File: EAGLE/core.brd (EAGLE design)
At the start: 20.3 x 33 mm, 47 parts, among them Q1 MMDT3904, U1 MIC5219, U3 STM32F10XCXT6, U4 SST25VF040B-50-4I-S2AF, X1 USB-MICROB, Y1 8Mhz

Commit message: Finished Core Debug v0.0.8
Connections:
- net SPI_MISO: no longer U2.SPI_DIN
- net SPI_MOSI: now also U2.SPI_DIN
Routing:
- net SPI_MISO: track 27.2 -> 26.7 mm
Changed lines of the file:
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@@
 <setting verticaltext="up"/>
 </settings>
-<grid distance="0.005" unitdist="inch" unit="inch" style="lines" multiple="1" display="yes" altdistance="0.005" altunitdist="inch" altunit="inch"/>
+<grid distance="0.05" unitdist="inch" unit="inch" style="lines" multiple="1" display="yes" altdistance="0.005" altunitdist="inch" altunit="inch"/>
 <layers>
-<layer number="1" name="Top" color="4" fill="1" visible="no" active="yes"/>
+<layer number="1" name="Top" color="4" fill="1" visible="yes" active="yes"/>
 <layer number="2" name="$GND" color="13" fill="1" visible="no" active="yes"/>
 <layer number="3" name="Route3" color="4" fill="3" visible="no" active="no"/>
@@
 <layer number="14" name="Route14" color="1" fill="6" visible="no" active="no"/>
 <layer number="15" name="$+3V3" color="11" fill="1" visible="no" active="yes"/>
-<layer number="16" name="Bottom" color="1" fill="1" visible="no" active="yes"/>
+<layer number="16" name="Bottom" color="1" fill="1" visible="yes" active="yes"/>
 <layer number="17" name="Pads" color="2" fill="1" visible="yes" active="yes"/>
-<layer number="18" name="Vias" color="2" fill="1" visible="no" active="yes"/>
-<layer number="19" name="Unrouted" color="6" fill="1" visible="no" active="yes"/>
+<layer number="18" name="Vias" color="2" fill="1" visible="yes" active="yes"/>
+<layer number="19" name="Unrouted" color="6" fill="1" visible="yes" active="yes"/>
 <layer number="20" name="Dimension" color="6" fill="1" visible="yes" active="yes"/>
 <layer number="21" name="tPlace" color="16" fill="1" visible="yes" active="yes"/>
-<layer number="22" name="bPlace" color="14" fill="1" visible="no" active="yes"/>
+<layer number="22" name="bPlace" color="14" fill="1" visible="yes" active="yes"/>
 <layer number="23" name="tOrigins" color="15" fill="1" visible="yes" active="yes"/>
-<layer number="24" name="bOrigins" color="15" fill="1" visible="no" active="yes"/>
+<layer number="24" name="bOrigins" color="15" fill="1" visible="yes" active="yes"/>
 <layer number="25" name="tNames" color="7" fill="1" visible="no" active="yes"/>
 <layer number="26" name="bNames" color="7" fill="1" visible="no" active="yes"/>
-<layer number="27" name="tValues" color="7" fill="1" visible="yes" active="yes"/>
+<layer number="27" name="tValues" color="7" fill="1" visible="no" active="yes"/>
 <layer number="28" name="bValues" color="7" fill="1" visible="no" active="yes"/>
 <layer number="29" name="tStop" color="7" fill="3" visible="no" active="yes"/>
 <layer number="30" name="bStop" color="7" fill="6" visible="no" active="yes"/>
-<layer number="31" name="tCream" color="7" fill="4" visible="yes" active="yes"/>
+<layer number="31" name="tCream" color="7" fill="4" visible="no" active="yes"/>
 <layer number="32" name="bCream" color="7" fill="5" visible="no" active="yes"/>
 <layer number="33" name="tFinish" color="6" fill="3" visible="no" active="yes"/>
@@
 <signal name="SPI_MISO">
 <contactref element="U2" pad="SPI_DOUT"/>
-<contactref element="U2" pad="SPI_DIN"/>
 <contactref element="U3" pad="27"/>
 <contactref element="U4" pad="2"/>
@@
 <wire x1="11.938" y1="18.034" x2="11.938" y2="18.161" width="0.2032" layer="1"/>
 <wire x1="11.938" y1="18.161" x2="11.43" y2="18.669" width="0.2032" layer="1"/>
-<wire x1="9.56" y1="19.92" x2="9.56" y2="20.482" width="0.2032" layer="1"/>
 <wire x1="9.56" y1="20.482" x2="9.906" y2="20.828" width="0.2032" layer="1"/>
 <wire x1="9.906" y1="20.828" x2="11.684" y2="20.828" width="0.2032" layer="1"/>
@@
 <wire x1="10.16" y1="17.653" x2="10.287" y2="17.526" width="0.2032" layer="16"/>
 <wire x1="10.287" y1="17.526" x2="11.43" y2="17.526" width="0.2032" layer="16"/>
+<contactref element="U2" pad="SPI_DIN"/>
+<wire x1="10.16" y1="17.653" x2="9.56" y2="19.92" width="0" layer="19" extent="1-16"/>
 </signal>
 <signal name="USB_DISC">

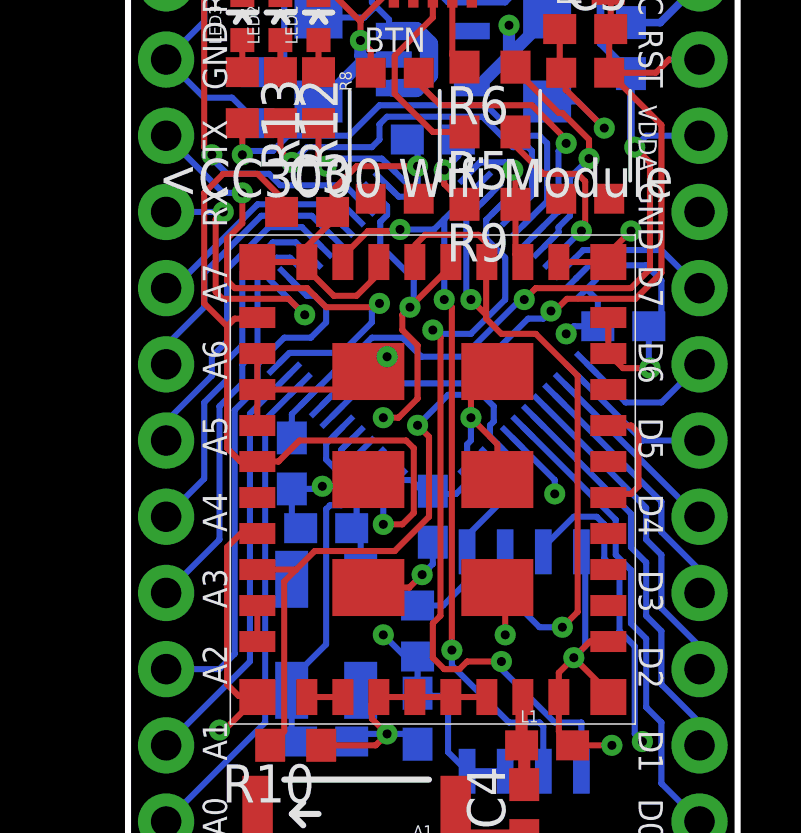
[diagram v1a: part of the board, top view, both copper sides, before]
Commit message: Fixed MOSI/MISO error in Core
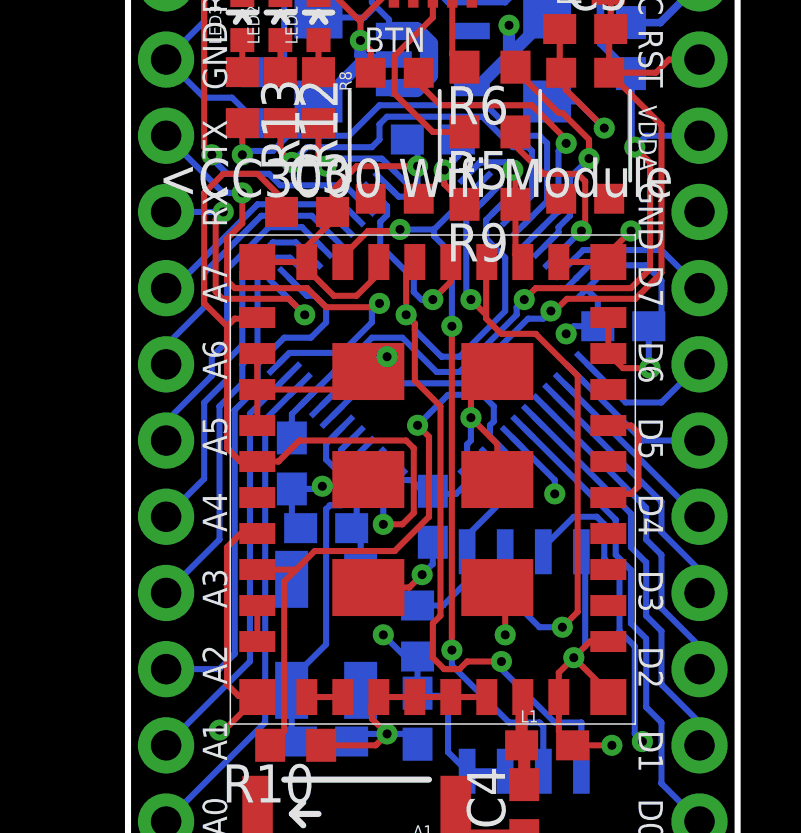
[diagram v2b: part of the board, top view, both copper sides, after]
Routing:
- net WIFI_INT: track 11.4 -> 6.25 mm, vias 2 -> 1
- net SPI_MOSI: track 25.6 -> 30.4 mm
- net SPI_MISO: track 26.7 -> 23.4 mm
- net VDDA: track 30.6 -> 31.2 mm
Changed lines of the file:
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@@
 <setting verticaltext="up"/>
 </settings>
-<grid distance="0.05" unitdist="inch" unit="inch" style="lines" multiple="1" display="yes" altdistance="0.005" altunitdist="inch" altunit="inch"/>
+<grid distance="0.005" unitdist="inch" unit="mm" style="lines" multiple="1" display="yes" altdistance="0.005" altunitdist="inch" altunit="inch"/>
 <layers>
 <layer number="1" name="Top" color="4" fill="1" visible="yes" active="yes"/>
@@
 <contactref element="U3" pad="26"/>
 <contactref element="U4" pad="6"/>
-<wire x1="10.541" y1="18.669" x2="10.541" y2="21.342978125" width="0.2032" layer="16"/>
 <wire x1="13.716" y1="4.572" x2="12.7" y2="4.572" width="0.2032" layer="16"/>
 <wire x1="13.843" y1="4.445" x2="13.716" y2="4.572" width="0.2032" layer="16"/>
 <wire x1="13.843" y1="2.9464" x2="13.843" y2="4.445" width="0.2032" layer="16"/>
-<via x="10.541" y="18.669" extent="1-16" drill="0.3"/>
 <wire x1="7.16" y1="19.92" x2="7.16" y2="20.368" width="0.2032" layer="1"/>
-<wire x1="10.541" y1="18.669" x2="10.795" y2="18.415" width="0.2032" layer="1"/>
-<wire x1="10.795" y1="18.415" x2="10.795" y2="6.985" width="0.2032" layer="1"/>
-<wire x1="11.750990625" y1="22.55296875" x2="10.541" y2="21.342978125" width="0.2032" layer="16"/>
+<wire x1="11.750990625" y1="22.55296875" x2="10.203821875" y2="21.0058" width="0.2032" layer="16"/>
 <wire x1="7.239" y1="19.999" x2="7.16" y2="19.92" width="0.2032" layer="1"/>
 <via x="10.795" y="6.985" extent="1-16" drill="0.3"/>
@@
 <via x="9.0678" y="21.0058" extent="1-16" drill="0.3"/>
 <wire x1="9.0678" y1="21.0058" x2="10.203821875" y2="21.0058" width="0.2032" layer="16"/>
-<wire x1="10.203821875" y1="21.0058" x2="10.541" y2="21.342978125" width="0.2032" layer="16"/>
 <wire x1="7.239" y1="19.999" x2="7.239" y2="20.193" width="0.2032" layer="1"/>
 <wire x1="7.239" y1="20.193" x2="8.001" y2="20.955" width="0.2032" layer="1"/>
 <wire x1="8.001" y1="20.955" x2="9.017" y2="20.955" width="0.2032" layer="1"/>
 <wire x1="9.017" y1="20.955" x2="9.0678" y2="21.0058" width="0.2032" layer="1"/>
+<via x="10.795" y="17.78" extent="1-16" drill="0.3"/>
+<wire x1="10.203821875" y1="21.0058" x2="10.203821875" y2="20.784178125" width="0.2032" layer="16"/>
+<wire x1="10.203821875" y1="20.784178125" x2="10.795" y2="20.193" width="0.2032" layer="16"/>
+<wire x1="10.795" y1="20.193" x2="10.795" y2="17.78" width="0.2032" layer="16"/>
+<wire x1="10.795" y1="6.985" x2="10.795" y2="17.78" width="0.2032" layer="1"/>
 </signal>
 <signal name="SPI_MISO">
@@
 <wire x1="11.938" y1="18.034" x2="11.938" y2="18.161" width="0.2032" layer="1"/>
 <wire x1="11.938" y1="18.161" x2="11.43" y2="18.669" width="0.2032" layer="1"/>
-<wire x1="9.56" y1="20.482" x2="9.906" y2="20.828" width="0.2032" layer="1"/>
-<wire x1="9.906" y1="20.828" x2="11.684" y2="20.828" width="0.2032" layer="1"/>
-<wire x1="11.684" y1="20.828" x2="11.938" y2="20.574" width="0.2032" layer="1"/>
-<wire x1="11.938" y1="20.574" x2="11.938" y2="19.942" width="0.2032" layer="1"/>
-<wire x1="11.938" y1="19.942" x2="11.96" y2="19.92" width="0.2032" layer="1"/>
 </signal>
 <signal name="OSC1">
@@
 <signal name="WIFI_INT">
 <contactref element="U2" pad="SPI_IRQ"/>
-<wire x1="10.76" y1="19.92" x2="10.76" y2="19.777" width="0.2032" layer="1"/>
-<wire x1="9.144" y1="18.161" x2="9.144" y2="17.653" width="0.2032" layer="1"/>
-<wire x1="9.144" y1="17.653" x2="9.652" y2="17.145" width="0.2032" layer="1"/>
-<via x="8.509" y="14.732" extent="1-16" drill="0.3"/>
-<wire x1="9.652" y1="17.145" x2="9.652" y2="15.367" width="0.2032" layer="1"/>
-<wire x1="9.652" y1="15.367" x2="9.017" y2="14.732" width="0.2032" layer="1"/>
-<wire x1="9.017" y1="14.732" x2="8.509" y2="14.732" width="0.2032" layer="1"/>
 <contactref element="U3" pad="22"/>
 <wire x1="8.215459375" y1="22.199415625" x2="8.636" y2="21.778875" width="0.2032" layer="16"/>
 <wire x1="8.636" y1="21.778875" x2="8.636" y2="21.4884" width="0.2032" layer="16"/>
-<wire x1="9.144" y1="18.161" x2="9.398" y2="18.415" width="0.2032" layer="1"/>
-<via x="9.398" y="18.415" extent="1-16" drill="0.3"/>
-<wire x1="9.398" y1="18.415" x2="9.525" y2="18.542" width="0.2032" layer="16"/>
-<wire x1="9.525" y1="18.542" x2="9.525" y2="19.3548" width="0.2032" layer="16"/>
-<wire x1="10.76" y1="19.777" x2="9.398" y2="18.415" width="0.2032" layer="1"/>
 <wire x1="8.636" y1="21.4884" x2="8.4074" y2="21.2598" width="0.2032" layer="16"/>
 <wire x1="8.4074" y1="21.2598" x2="8.4074" y2="20.4724" width="0.2032" layer="16"/>
 <wire x1="9.525" y1="19.3548" x2="8.4074" y2="20.4724" width="0.2032" layer="16"/>
+<wire x1="9.525" y1="19.3548" x2="9.525" y2="18.923" width="0.2032" layer="16"/>
+<via x="10.16" y="18.669" extent="1-16" drill="0.3"/>
+<wire x1="9.525" y1="18.923" x2="9.779" y2="18.669" width="0.2032" layer="16"/>
+<wire x1="9.779" y1="18.669" x2="10.16" y2="18.669" width="0.2032" layer="16"/>
+<wire x1="10.76" y1="19.92" x2="10.76" y2="19.269" width="0.2032" layer="1"/>
+<wire x1="10.76" y1="19.269" x2="10.16" y2="18.669" width="0.2032" layer="1"/>
 </signal>
 <signal name="WIFI_EN">
@@
 <wire x1="15.113" y1="4.572" x2="15.113" y2="2.9464" width="0.2032" layer="16"/>
 <wire x1="14.224" y1="4.572" x2="15.113" y2="4.572" width="0.2032" layer="16"/>
-<wire x1="10.414" y1="8.128" x2="10.414" y2="17.399" width="0.2032" layer="1"/>
 <wire x1="12.4581" y1="21.8458625" x2="11.938" y2="21.3257625" width="0.2032" layer="16"/>
 <wire x1="11.049" y1="6.35" x2="11.303" y2="6.604" width="0.2032" layer="1"/>
@@
 <wire x1="11.938" y1="21.3257625" x2="11.938" y2="20.701" width="0.2032" layer="16"/>
 <wire x1="11.938" y1="20.701" x2="12.573" y2="20.066" width="0.2032" layer="16"/>
-<wire x1="12.573" y1="20.066" x2="12.573" y2="18.669" width="0.2032" layer="16"/>
-<wire x1="12.573" y1="18.669" x2="11.43" y2="17.526" width="0.2032" layer="16"/>
-<wire x1="10.414" y1="17.399" x2="10.16" y2="17.653" width="0.2032" layer="1"/>
-<via x="10.16" y="17.653" extent="1-16" drill="0.3"/>
-<wire x1="10.16" y1="17.653" x2="10.287" y2="17.526" width="0.2032" layer="16"/>
-<wire x1="10.287" y1="17.526" x2="11.43" y2="17.526" width="0.2032" layer="16"/>
+<wire x1="12.573" y1="20.066" x2="12.573" y2="18.288" width="0.2032" layer="16"/>
 <contactref element="U2" pad="SPI_DIN"/>
-<wire x1="10.16" y1="17.653" x2="9.56" y2="19.92" width="0" layer="19" extent="1-16"/>
+<wire x1="9.56" y1="15.967" x2="10.414" y2="15.113" width="0.2032" layer="1"/>
+<wire x1="10.414" y1="15.113" x2="10.414" y2="8.128" width="0.2032" layer="1"/>
+<via x="9.271" y="18.161" extent="1-16" drill="0.3"/>
+<wire x1="9.56" y1="15.967" x2="9.56" y2="17.872" width="0.2032" layer="1"/>
+<wire x1="9.56" y1="17.872" x2="9.271" y2="18.161" width="0.2032" layer="1"/>
+<wire x1="12.573" y1="18.288" x2="11.049" y2="16.764" width="0.2032" layer="16"/>
+<wire x1="11.049" y1="16.764" x2="10.449" y2="16.764" width="0.2032" layer="16"/>
+<wire x1="10.449" y1="16.764" x2="9.56" y2="17.653" width="0.2032" layer="16"/>
+<wire x1="9.56" y1="17.653" x2="9.56" y2="17.872" width="0.2032" layer="16"/>
+<wire x1="9.56" y1="17.872" x2="9.271" y2="18.161" width="0.2032" layer="16"/>
+<wire x1="9.271" y1="18.161" x2="9.271" y2="19.631" width="0.2032" layer="1"/>
+<wire x1="9.271" y1="19.631" x2="9.56" y2="19.92" width="0.2032" layer="1"/>
 </signal>
 <signal name="USB_DISC">
@@
 <wire x1="6.985" y1="16.256" x2="8.128" y2="17.399" width="0.2032" layer="16"/>
 <wire x1="8.128" y1="17.399" x2="9.144" y2="17.399" width="0.2032" layer="16"/>
-<wire x1="9.144" y1="17.399" x2="9.779" y2="16.764" width="0.2032" layer="16"/>
-<wire x1="9.779" y1="16.764" x2="11.176" y2="16.764" width="0.2032" layer="16"/>
-<wire x1="11.176" y1="16.764" x2="13.081" y2="18.669" width="0.2032" layer="16"/>
-<wire x1="13.081" y1="18.669" x2="13.208" y2="18.669" width="0.2032" layer="16"/>
+<wire x1="9.144" y1="17.399" x2="10.287" y2="16.256" width="0.2032" layer="16"/>
 <via x="13.208" y="18.669" extent="1-16" drill="0.3"/>
 <wire x1="13.208" y1="18.669" x2="13.589" y2="19.05" width="0.2032" layer="1"/>
@@
 <wire x1="16.764" y1="26.201" x2="16.764" y2="23.876" width="0.254" layer="16"/>
 <wire x1="16.764" y1="23.876" x2="16.891" y2="23.749" width="0.254" layer="16"/>
+<wire x1="10.287" y1="16.256" x2="11.049" y2="16.256" width="0.2032" layer="16"/>
+<wire x1="11.049" y1="16.256" x2="12.954" y2="18.161" width="0.2032" layer="16"/>
+<wire x1="12.954" y1="18.161" x2="12.954" y2="18.415" width="0.2032" layer="16"/>
+<wire x1="12.954" y1="18.415" x2="13.208" y2="18.669" width="0.2032" layer="16"/>
 </signal>
 <signal name="N$8">
@@
 </signal>
 </signals>
+<errors>
+</errors>
 </board>
 </drawing>

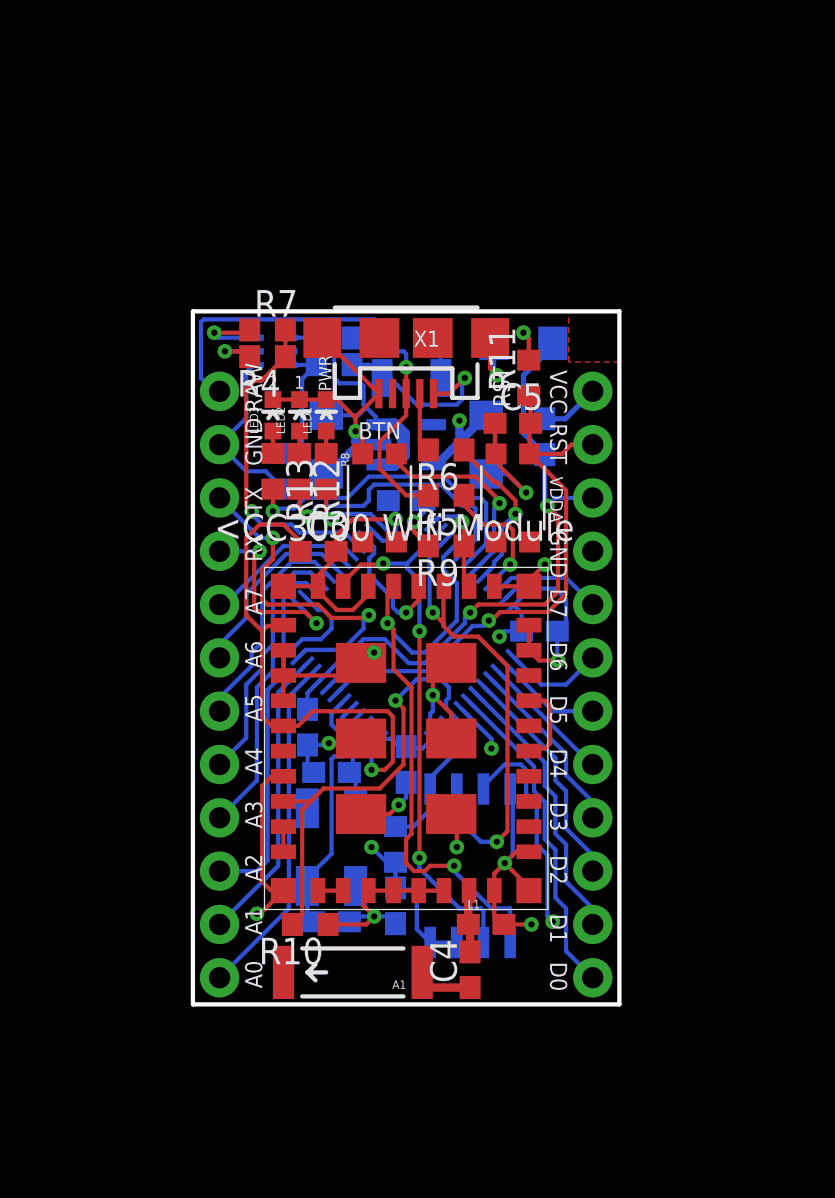
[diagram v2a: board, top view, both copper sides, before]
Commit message: Better USB, improved power layout, got rid of resistor near antenna
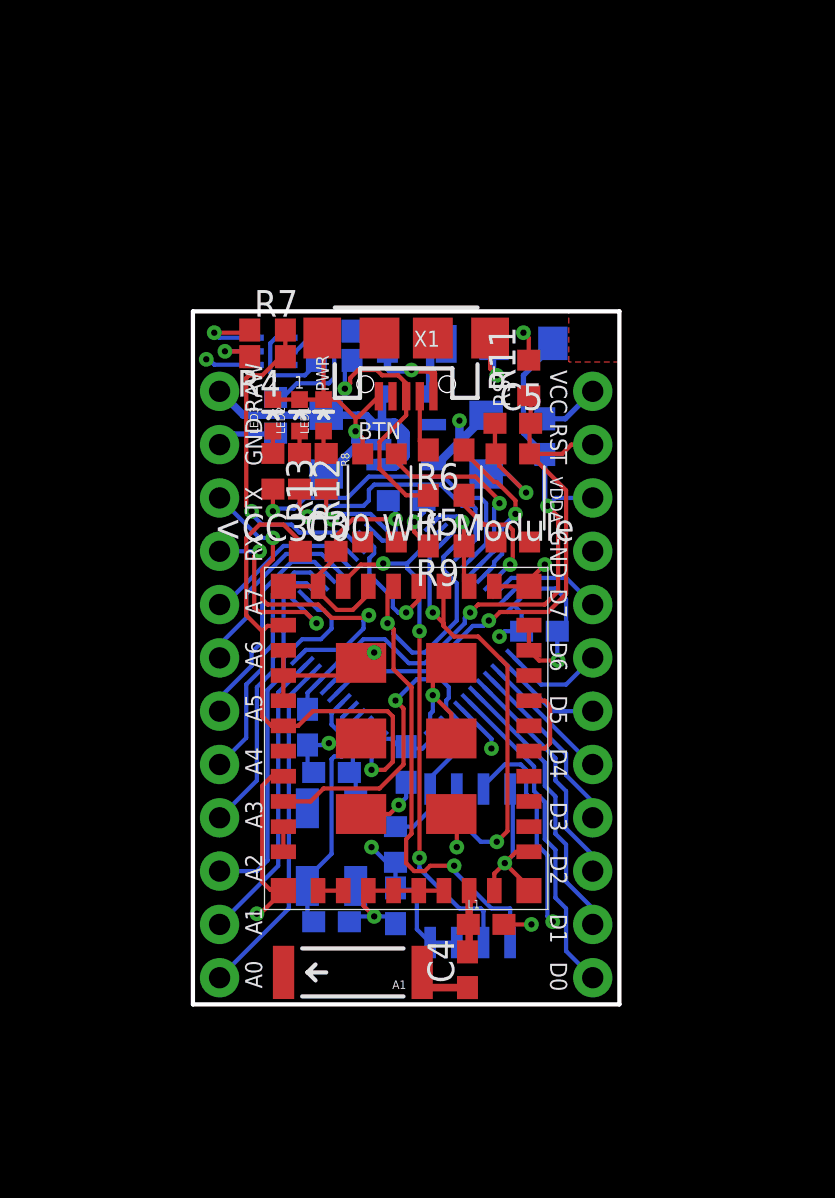
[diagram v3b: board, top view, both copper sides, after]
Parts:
- removed R10: 10K, rcl:R0603
- X1: value USB-MICROB -> USBUSB-MICROB-ALIGN; device SparkFun-Connectors:USB-MICROB -> Spark:USB-MICROB-ALIGN
- moved D1 2.79 mm to (10.2, 29.1)
- moved R2 2.69 mm to (3.94, 28.1)
- moved F1 1.65 mm to (10.7, 31.5)
- moved R1 1.60 mm to (6.73, 32.1)
- moved R3 1.07 mm to (6.73, 30.7)
- moved C4 0.13 mm to (13.1, 1.65)
- moved LED1 0.13 mm to (6.22, 28.1)
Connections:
- net GND: no longer R10.1
- net WIFI_EN: no longer R10.2
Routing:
- net RAW: track 25.5 -> 13.6 mm
- net GND: track 120.7 -> 112.6 mm, vias 16 -> 17
- net WIFI_EN: track 20.6 -> 14.4 mm
- net N$16: track 1.39 -> 4.96 mm
- net UVCC: track 9.01 -> 6.46 mm
- net N$1: track 11.7 -> 13.9 mm
- net N$13: track 7.27 -> 8.62 mm
- net N$3: track 2.24 -> 2.97 mm
